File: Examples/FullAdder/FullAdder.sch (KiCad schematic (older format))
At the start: 13 parts, among them U1 plot_v1, U2 plot_v1, U3 plot_v1, U4 plot_v1, U5 plot_v1, U6 adc_bridge_3, U7 dac_bridge_2, X1 full_adder

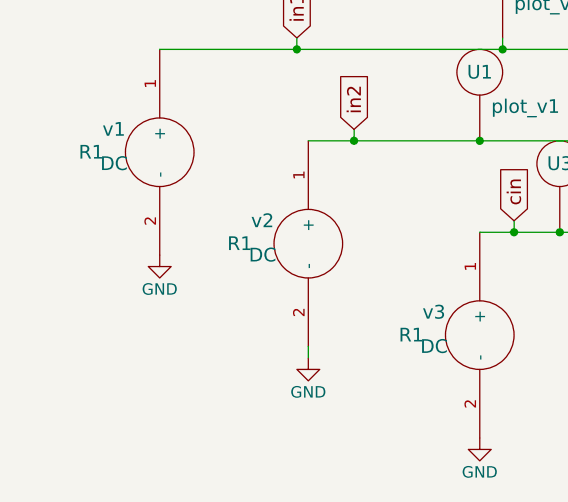
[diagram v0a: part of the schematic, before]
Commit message: resolved kicadToNgSpice
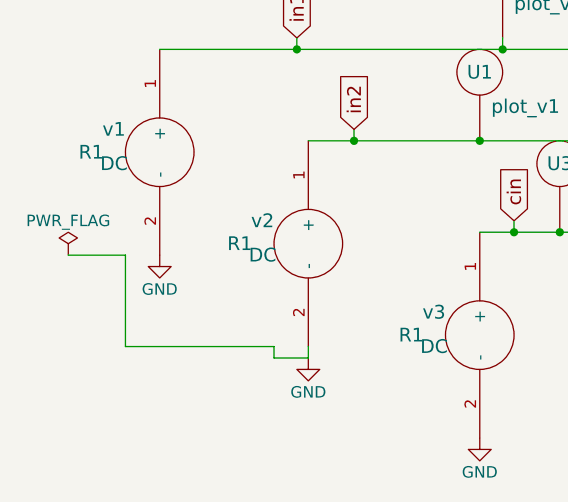
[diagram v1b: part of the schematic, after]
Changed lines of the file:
@@
 LIBS:74xx
 LIBS:cmos4000
+LIBS:FullAdder-cache
 EELAYER 25 0
 EELAYER END
@@
 Wire Wire Line
 	1950 4400 1950 4450
+$Comp
+L PWR_FLAG #FLG06
+U 1 1 5CEE2E64
+P 900 4000
+F 0 "#FLG06" H 900 4075 50  0001 C CNN
+F 1 "PWR_FLAG" H 900 4150 50  0000 C CNN
+F 2 "" H 900 4000 50  0001 C CNN
+F 3 "" H 900 4000 50  0001 C CNN
+	1    900  4000
+	1    0    0    -1
+$EndComp
+Wire Wire Line
+	900  4000 1150 4000
+Wire Wire Line
+	1150 4000 1150 4400
+Wire Wire Line
+	1150 4400 1800 4400
+Wire Wire Line
+	1800 4400 1800 4450
+Wire Wire Line
+	1800 4450 1950 4450
 $EndSCHEMATC

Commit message: Examples pulled from original
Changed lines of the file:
@@
 LIBS:74xx
 LIBS:cmos4000
-LIBS:FullAdder-cache
 EELAYER 25 0
 EELAYER END
@@
 Wire Wire Line
 	1950 4400 1950 4450
-$Comp
-L PWR_FLAG #FLG06
-U 1 1 5CEE2E64
-P 900 4000
-F 0 "#FLG06" H 900 4075 50  0001 C CNN
-F 1 "PWR_FLAG" H 900 4150 50  0000 C CNN
-F 2 "" H 900 4000 50  0001 C CNN
-F 3 "" H 900 4000 50  0001 C CNN
-	1    900  4000
-	1    0    0    -1
-$EndComp
-Wire Wire Line
-	900  4000 1150 4000
-Wire Wire Line
-	1150 4000 1150 4400
-Wire Wire Line
-	1150 4400 1800 4400
-Wire Wire Line
-	1800 4400 1800 4450
-Wire Wire Line
-	1800 4450 1950 4450
 $EndSCHEMATC
